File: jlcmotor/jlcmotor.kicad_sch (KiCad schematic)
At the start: 15 parts, among them J1 ScrewTerminal, U1 PinHeader8, U2 PinHeader8

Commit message: bulk capacitor
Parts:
- added C1: (no value), Capacitor_SMD:C_1206_3216Metric, symbol Device:C
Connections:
- net GND: now also C1.2
- net VMOT: now also C1.1
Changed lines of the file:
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@@
+  (wire
+    (pts
+      (xy 62.23 27.94)
+      (xy 62.23 25.4)
+    )
+    (stroke
+      (width 0)
+      (type default)
+    )
+  )
+  (wire
+    (pts
+      (xy 46.99 17.78)
+      (xy 46.99 20.32)
+    )
+    (stroke
+      (width 0)
+      (type default)
+    )
+  )
   (wire
     (pts
@@
   (wire
     (pts
+      (xy 62.23 20.32)
+      (xy 62.23 17.78)
+    )
+    (stroke
+      (width 0)
+      (type default)
+    )
+  )
+  (wire
+    (pts
       (xy 99.06 69.85)
       (xy 99.06 54.61)
@@
     )
   )
+  (label "GND"
+    (at 97.79 31.75 180)
+    (effects
+      (font
+        (size 1.27 1.27)
+      )
+      (justify right bottom)
+    )
+  )
   (label "5V"
     (at 82.55 55.88 180)
@@
     )
   )
+  (label "3V3"
+    (at 97.79 34.29 180)
+    (effects
+      (font
+        (size 1.27 1.27)
+      )
+      (justify right bottom)
+    )
+  )
+  (label "GND"
+    (at 62.23 27.94 180)
+    (effects
+      (font
+        (size 1.27 1.27)
+      )
+      (justify right bottom)
+    )
+  )
+  (label "5V"
+    (at 46.99 17.78 180)
+    (effects
+      (font
+        (size 1.27 1.27)
+      )
+      (justify right bottom)
+    )
+  )
+  (label "GND"
+    (at 46.99 25.4 180)
+    (effects
+      (font
+        (size 1.27 1.27)
+      )
+      (justify right bottom)
+    )
+  )
   (label "GND"
     (at 125.73 69.85 180)
@@
     )
   )
+  (label "5V"
+    (at 97.79 29.21 180)
+    (effects
+      (font
+        (size 1.27 1.27)
+      )
+      (justify right bottom)
+    )
+  )
   (label "VMOT"
     (at 125.73 67.31 180)
@@
   (label "CANL"
     (at 48.26 44.45 180)
+    (effects
+      (font
+        (size 1.27 1.27)
+      )
+      (justify right bottom)
+    )
+  )
+  (label "12V"
+    (at 62.23 20.32 180)
     (effects
       (font
@@
   )
   (symbol
+    (lib_id "Device:C")
+    (at 130.81 66.04 0)
+    (unit 1)
+    (exclude_from_sim no)
+    (in_bom yes)
+    (on_board yes)
+    (dnp no)
+    (property "Reference" "C1"
+      (at 135.128 66.04 0)
+      (effects
+        (font
+          (size 1.27 1.27)
+        )
+        (justify left)
+      )
+    )
+    (property "Value" ""
+      (at 130.81 66.04 0)
+      (effects
+        (font
+          (size 1.27 1.27)
+        )
+      )
+    )
+    (property "Footprint" "Capacitor_SMD:C_1206_3216Metric"
+      (at 57.1499 2.5399 0)
+      (effects
+        (font
+          (size 1.27 1.27)
+        )
+        (hide yes)
+      )
+    )
+    (property "Datasheet" ""
+      (at 130.81 66.04 0)
+      (effects
+        (font
+          (size 1.27 1.27)
+        )
+      )
+    )
+    (property "Description" ""
+      (at 130.81 66.04 0)
+      (effects
+        (font
+          (size 1.27 1.27)
+        )
+      )
+    )
+    (property "lcsc" "C76659"
+      (at 57.1499 2.5399 0)
+      (effects
+        (font
+          (size 1.27 1.27)
+        )
+        (hide yes)
+      )
+    )
+    (pin "1"
+    )
+    (pin "2"
+    )
+    (instances
+      (project ""
+        (path "/0c4a29c7-ab23-4ca5-9754-897574cc5995"
+          (reference "C1")
+          (unit 1)
+        )
+      )
+    )
+  )
+  (symbol
     (lib_id "Connector_Generic:Conn_01x02")
     (at 52.07 25.4 0)
@@
     )
   )
-  (wire
-    (pts
-      (xy 62.23 27.94)
-      (xy 62.23 25.4)
-    )
-    (stroke
-      (width 0)
-      (type default)
-    )
-  )
-  (wire
-    (pts
-      (xy 62.23 20.32)
-      (xy 62.23 17.78)
-    )
-    (stroke
-      (width 0)
-      (type default)
-    )
-  )
-  (wire
-    (pts
-      (xy 46.99 17.78)
-      (xy 46.99 20.32)
-    )
-    (stroke
-      (width 0)
-      (type default)
-    )
-  )
-  (label "5V"
-    (at 97.78999999999999 29.209999999999997 180)
-    (effects
-      (font
-        (size 1.27 1.27)
-      )
-      (justify right bottom)
-    )
-  )
-  (label "3V3"
-    (at 97.78999999999999 34.29 180)
+  (label "VMOT"
+    (at 130.81 62.230000000000004 180)
     (effects
       (font
@@
   )
   (label "GND"
-    (at 97.78999999999999 31.75 180)
-    (effects
-      (font
-        (size 1.27 1.27)
-      )
-      (justify right bottom)
-    )
-  )
-  (label "12V"
-    (at 62.23 20.32 180)
-    (effects
-      (font
-        (size 1.27 1.27)
-      )
-      (justify right bottom)
-    )
-  )
-  (label "GND"
-    (at 62.23 27.94 180)
-    (effects
-      (font
-        (size 1.27 1.27)
-      )
-      (justify right bottom)
-    )
-  )
-  (label "5V"
-    (at 46.99 17.78 180)
-    (effects
-      (font
-        (size 1.27 1.27)
-      )
-      (justify right bottom)
-    )
-  )
-  (label "GND"
-    (at 46.99 25.4 180)
-    (effects
-      (font
+    (at 130.81 69.85000000000001 180)
+    (effects
+      (font

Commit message: limit sw
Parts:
- added C2, C3: (no value), Capacitor_SMD:C_0603_1608Metric, symbol Device:C
- added R2, R3: (no value), Resistor_SMD:R_0603_1608Metric, symbol Device:R
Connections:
- net 3V3: now also R2.1, R3.1
- net GND: now also J3.1 (Pin_1), J3.3 (Pin_3), C2.2, C3.2
- net at J3.2 (Pin_2): now also U1.3 (Pin_3), C2.1, R2.2
- net at J3.4 (Pin_4): now also U1.7 (Pin_7), C3.1, R3.2
- net at J2.3 (Pin_3): no longer names the net of J2.3 (Pin_3)
- net at J2.3 (Pin_3): no longer J2.4 (Pin_4)

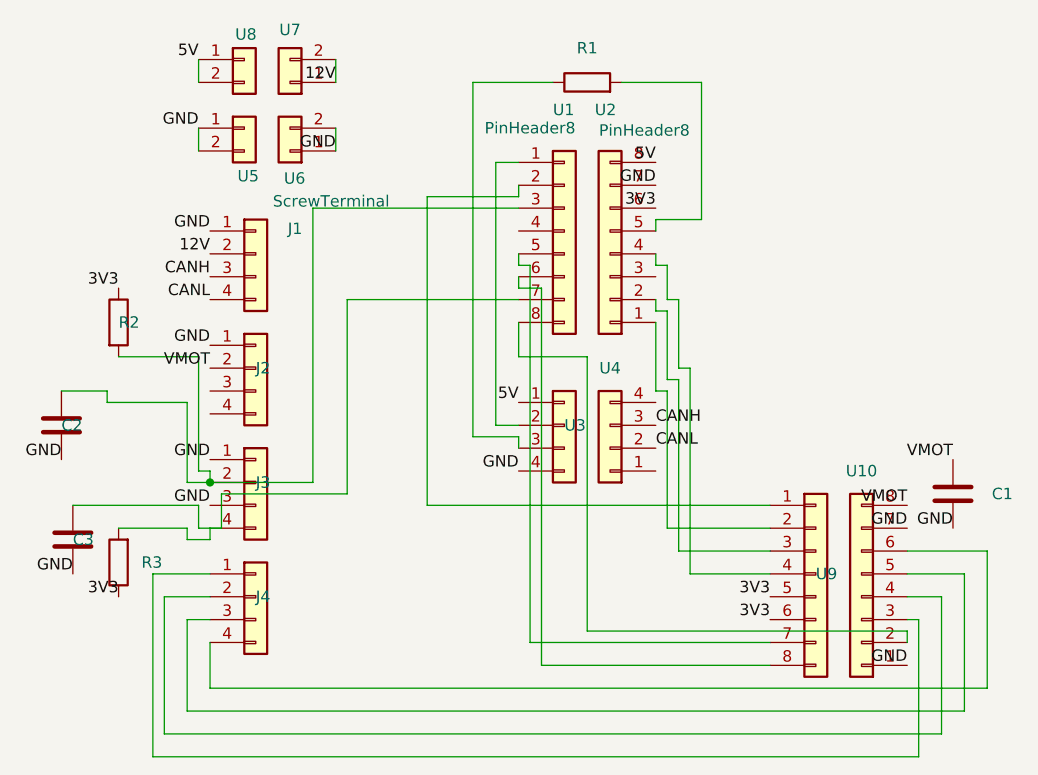
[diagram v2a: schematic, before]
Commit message: status led and power oring
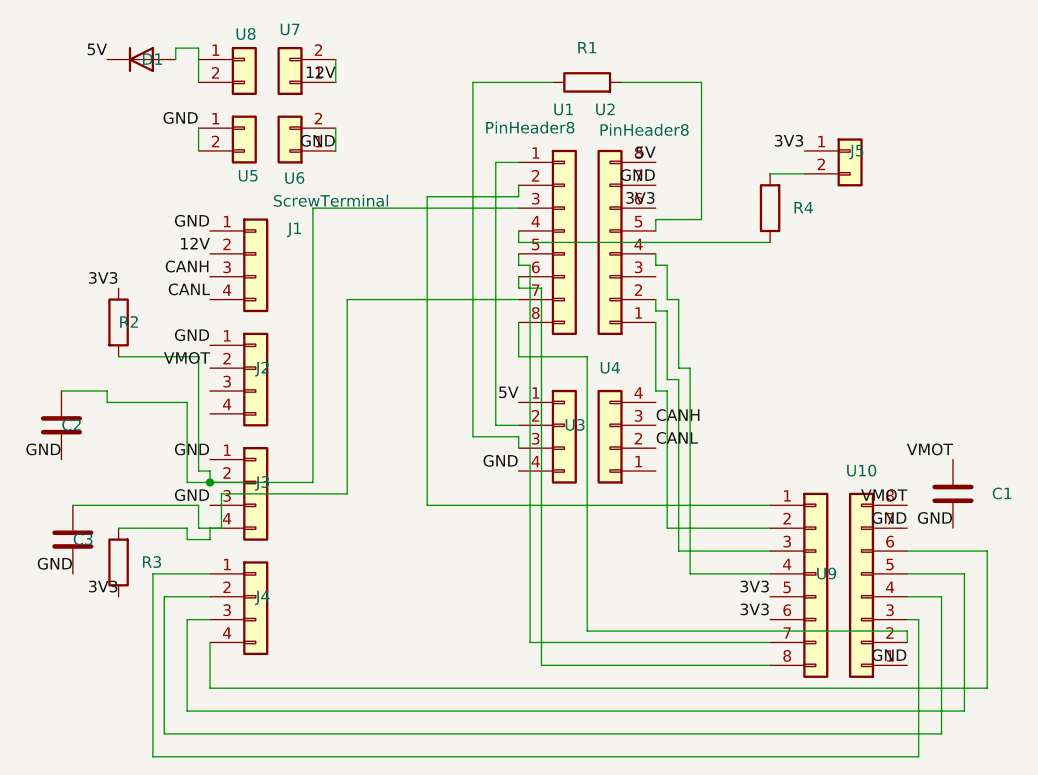
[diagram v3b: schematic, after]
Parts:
- added D1: (no value), Diode_SMD:D_SMA, symbol Device:D
- added J5: (no value), Connector_PinSocket_2.54mm:PinSocket_1x02_P2.54mm_Vertical, symbol Connector_Generic:Conn_01x02
- added R4: (no value), Resistor_SMD:R_0603_1608Metric, symbol Device:R
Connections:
- net 3V3: now also J5.1 (Pin_1)
- net 5V: now also D1.1 (K); no longer U8.1 (Pin_1), U8.2 (Pin_2)
- net at U1.4 (Pin_4): now also R4.1
- new net: J5.2 (Pin_2), R4.2
- new net: D1.2 (A), U8.1 (Pin_1), U8.2 (Pin_2)
